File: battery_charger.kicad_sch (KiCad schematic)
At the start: 20 parts, among them J8 Conn_01x04, U15 BQ25895RTW

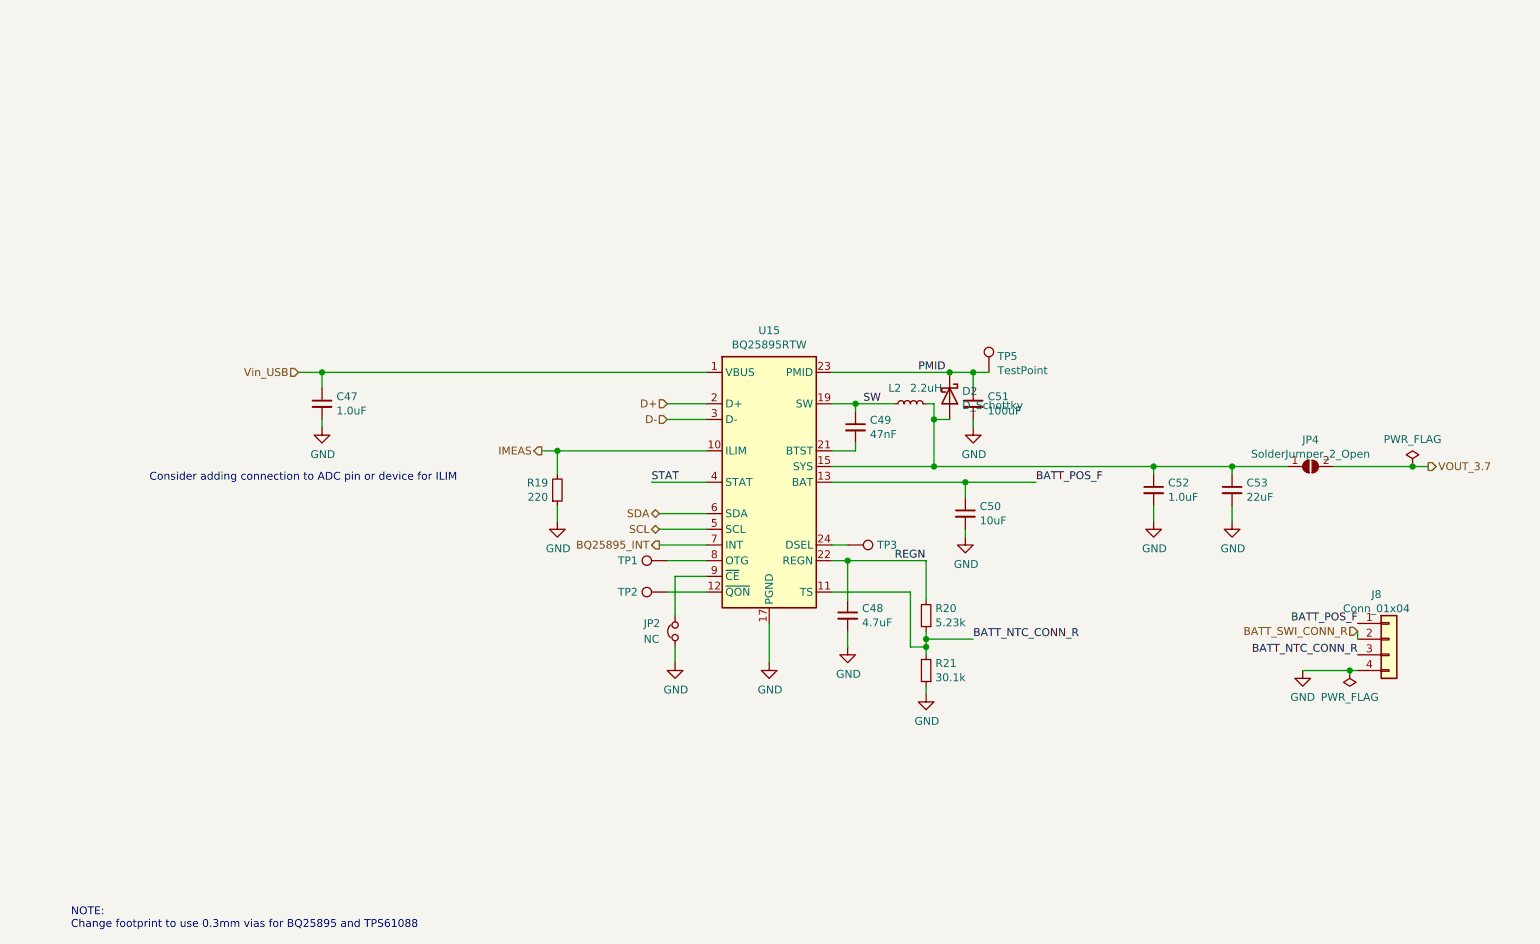
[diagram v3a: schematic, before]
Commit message: Lots of changes: add USB switch in charger circuit, reroute differential pairs using proper track widths; make CM4 courtyard the full size. Fixes #11.
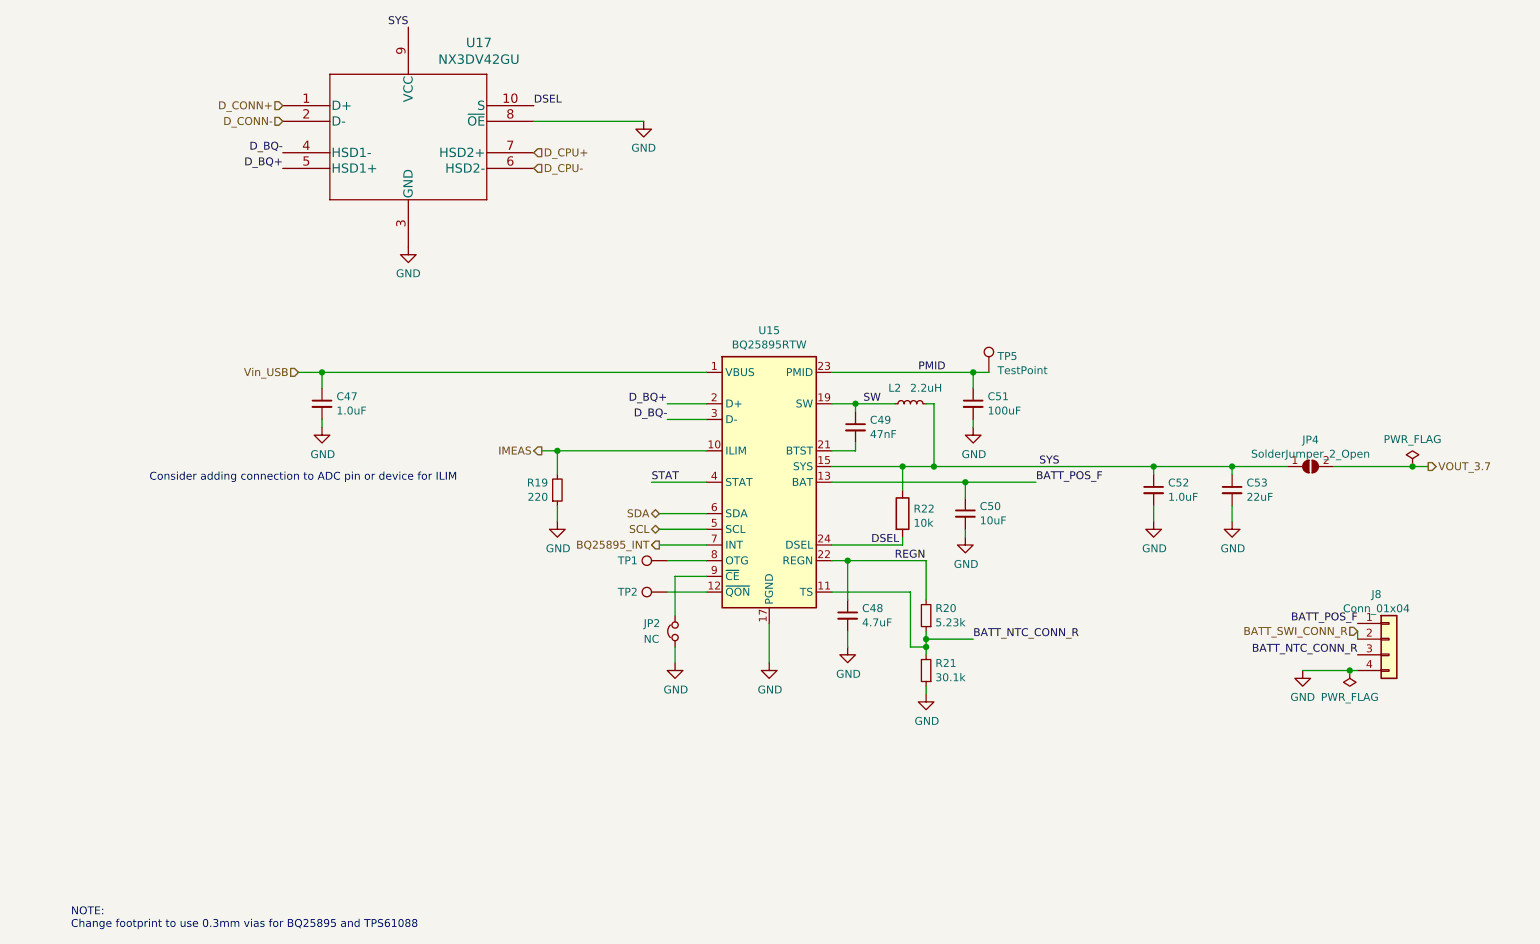
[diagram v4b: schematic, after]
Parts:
- removed D2: D_Schottky, footprints:NSR10F20NXT5G, symbol Device:D_Schottky
- removed TP3: DNP, TestPoint:TestPoint_Pad_1.0x1.0mm, symbol Connector:TestPoint
- added R22: 10k, Resistor_SMD:R_0402_1005Metric, symbol Device:R
- added U17: NX3DV42GU, footprints:NX3DV42GU, symbol NX3DV42:NX3DV42GU
- TP5: footprint (none) -> TestPoint:TestPoint_Pad_D1.0mm
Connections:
- net GND: now also U17.3 (GND), U17.8 (~OE)
- net SYS: now reaches C52.1, C53.1, JP4.1 (A), L2.2, U15.15 (SYS), U15.16 (SYS)
- net SYS: now also R22.1, U17.9 (VCC)
- net DSEL: now reaches U15.24 (DSEL)
- net DSEL: now also R22.2, U17.10 (S)
- net D+ renamed D_BQ+
- net D_BQ+: now also U17.5 (HSD1+)
- net D- renamed D_BQ-
- net D_BQ-: now also U17.4 (HSD1-)
- new net D_CONN+: U17.1 (D+)
- new net D_CONN-: U17.2 (D-)
- new net D_CPU+: U17.7 (HSD2+)
- new net D_CPU-: U17.6 (HSD2-)

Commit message: reroute LVDS diff pairs; add 5v boost converter. Fixes #1.
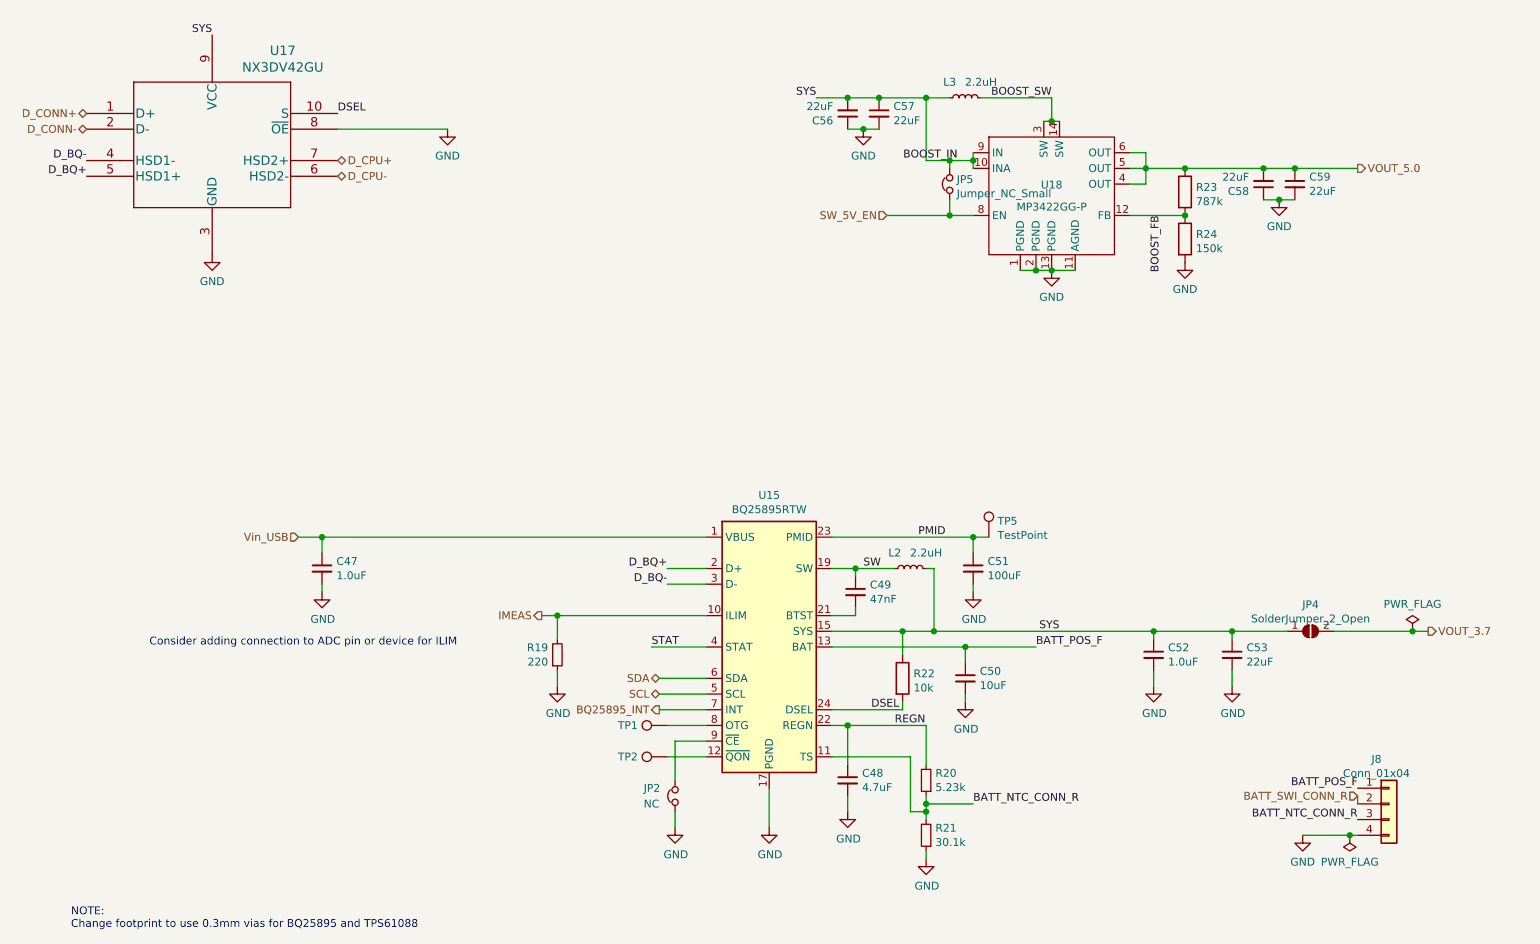
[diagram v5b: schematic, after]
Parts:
- added C56, C57, C58, C59: 22uF, Capacitor_SMD:C_0805_2012Metric, symbol Device:C_Small
- added JP5: Jumper_NC_Small, Resistor_SMD:R_0402_1005Metric, symbol Device:Jumper_NC_Small
- added L3: 2.2uH, Inductor_SMD:L_1008_2520Metric, symbol Device:L_Small
- added R23: 787k, Resistor_SMD:R_0402_1005Metric, symbol Device:R
- added R24: 150k, Resistor_SMD:R_0402_1005Metric, symbol Device:R
- added U18: MP3422GG-P, footprints:MP3422GG-P, symbol mp3422:MP3422GG-P
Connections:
- net GND: now also C56.1, C57.2, C58.1, C59.2, R24.2, U18.1 (PGND), U18.11 (AGND), U18.13 (PGND), U18.2 (PGND)
- net SYS renamed BOOST_IN
- net BOOST_IN: now also C56.2, C57.1, JP5.2, L3.1, U18.10 (INA), U18.9 (IN)
- new net BOOST_FB: R23.2, R24.1, U18.12 (FB)
- new net BOOST_SW: L3.2, U18.14 (SW), U18.3 (SW)
- new net SW_5V_EN: JP5.1, U18.8 (EN)
- new net VOUT_5.0: C58.2, C59.1, R23.1, U18.4 (OUT), U18.5 (OUT), U18.6 (OUT)
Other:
- moved on the sheet: C47, C48, C49, C50, C51, C52, C53, J8, JP2, JP4, L2, R19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

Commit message: Add datasheet for MP3422 boost converter
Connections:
- net BOOST_IN: now also JP5.1; no longer JP5.2
- net SW_5V_EN: now also JP5.2; no longer JP5.1
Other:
- moved on the sheet: JP5
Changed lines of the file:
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@@
     (pin "2")
   )
-  (symbol (lib_id "Device:Jumper_NC_Small") (at 172.72 46.99 90) (unit 1)
-    (in_bom yes) (on_board yes) (fields_autoplaced)
-    (property "Reference" "JP5" (id 0) (at 173.8631 46.2291 90)
-      (effects (font (size 1.27 1.27)) (justify right))
-    )
-    (property "Value" "Jumper_NC_Small" (id 1) (at 173.8631 48.5278 90)
-      (effects (font (size 1.27 1.27)) (justify right))
+  (symbol (lib_id "Device:Jumper_NC_Small") (at 172.72 46.99 270) (unit 1)
+    (in_bom yes) (on_board yes)
+    (property "Reference" "JP5" (id 0) (at 166.9289 46.2291 90)
+      (effects (font (size 1.27 1.27)) (justify left))
+    )
+    (property "Value" "Jumper_NC_Small" (id 1) (at 154.2289 48.5278 90)
+      (effects (font (size 1.27 1.27)) (justify left))
     )
     (property "Footprint" "Resistor_SMD:R_0402_1005Metric" (id 2) (at 172.72 46.99 0)
@@
       (effects (font (size 1.27 1.27)) hide)
     )
-    (property "Datasheet" "" (id 3) (at 189.23 49.53 0)
-      (effects (font (size 1.27 1.27)) hide)
-    )
+    (property "Datasheet" "${KIPRJMOD}/datasheets/MP3422.pdf" (id 3) (at 189.23 49.53 0)
+      (effects (font (size 1.27 1.27)) hide)
+    )

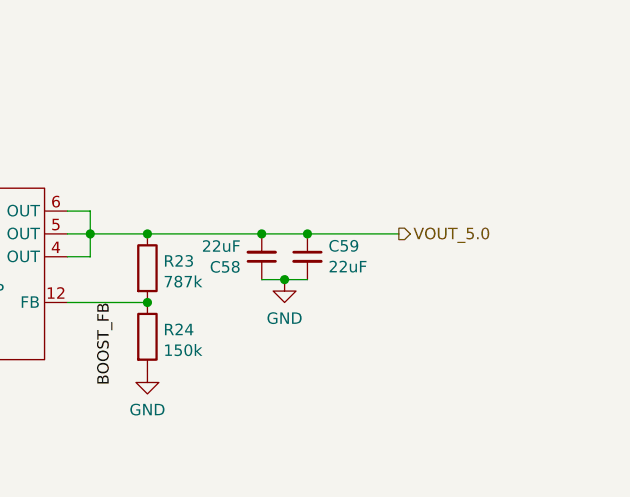
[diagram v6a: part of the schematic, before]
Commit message: Add jumper for 5V boost output.
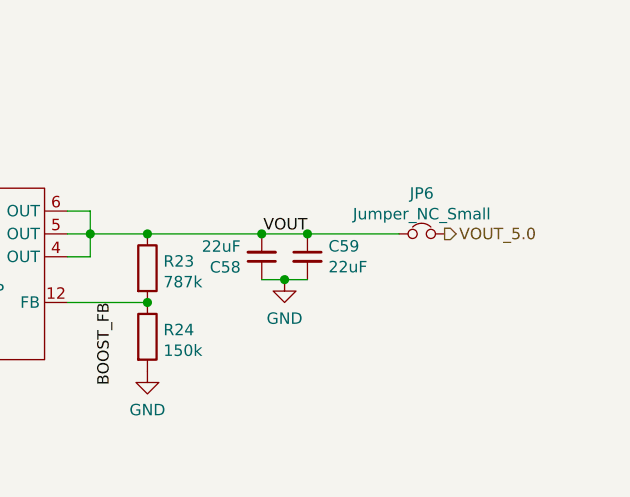
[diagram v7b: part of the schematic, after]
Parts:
- added JP6: Jumper_NC_Small, Resistor_SMD:R_0402_1005Metric, symbol Device:Jumper_NC_Small
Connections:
- net VOUT_5.0: now also JP6.2; no longer C58.2, C59.1, R23.1, U18.4 (OUT), U18.5 (OUT), U18.6 (OUT)
- new net VOUT: C58.2, C59.1, JP6.1, R23.1, U18.4 (OUT), U18.5 (OUT), U18.6 (OUT)
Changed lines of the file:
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@@
+    (effects (font (size 1.27 1.27)) (justify right bottom))
+  )
+  (label "VOUT" (at 228.6 44.45 180)
     (effects (font (size 1.27 1.27)) (justify right bottom))
   )
@@
     (effects (font (size 1.27 1.27)) (justify right))
   )
-  (hierarchical_label "VOUT_5.0" (shape output) (at 238.76 44.45 0)
+  (hierarchical_label "BATT_SWI_CONN_R" (shape input) (at 238.76 146.05 180)
+    (effects (font (size 1.27 1.27)) (justify right))
+  )
+  (hierarchical_label "VOUT_5.0" (shape output) (at 243.84 44.45 0)
     (effects (font (size 1.27 1.27)) (justify left))
-  )
-  (hierarchical_label "BATT_SWI_CONN_R" (shape input) (at 238.76 146.05 180)
-    (effects (font (size 1.27 1.27)) (justify right))
   )
   (hierarchical_label "VOUT_3.7" (shape output) (at 250.19 119.38 0)
@@
       (effects (font (size 1.27 1.27)) hide)
     )
+    (pin "1")
+    (pin "2")
+  )
+  (symbol (lib_id "Device:Jumper_NC_Small") (at 241.3 44.45 0) (unit 1)
+    (in_bom yes) (on_board yes) (fields_autoplaced)
+    (property "Reference" "JP6" (id 0) (at 241.3 39.95 0))
+    (property "Value" "Jumper_NC_Small" (id 1) (at 241.3 42.2487 0))
+    (property "Footprint" "Resistor_SMD:R_0402_1005Metric" (id 2) (at 241.3 44.45 0)
+      (effects (font (size 1.27 1.27)) hide)
+    )
+    (property "Datasheet" "~" (id 3) (at 241.3 44.45 0)
+      (effects (font (size 1.27 1.27)) hide)
+    )

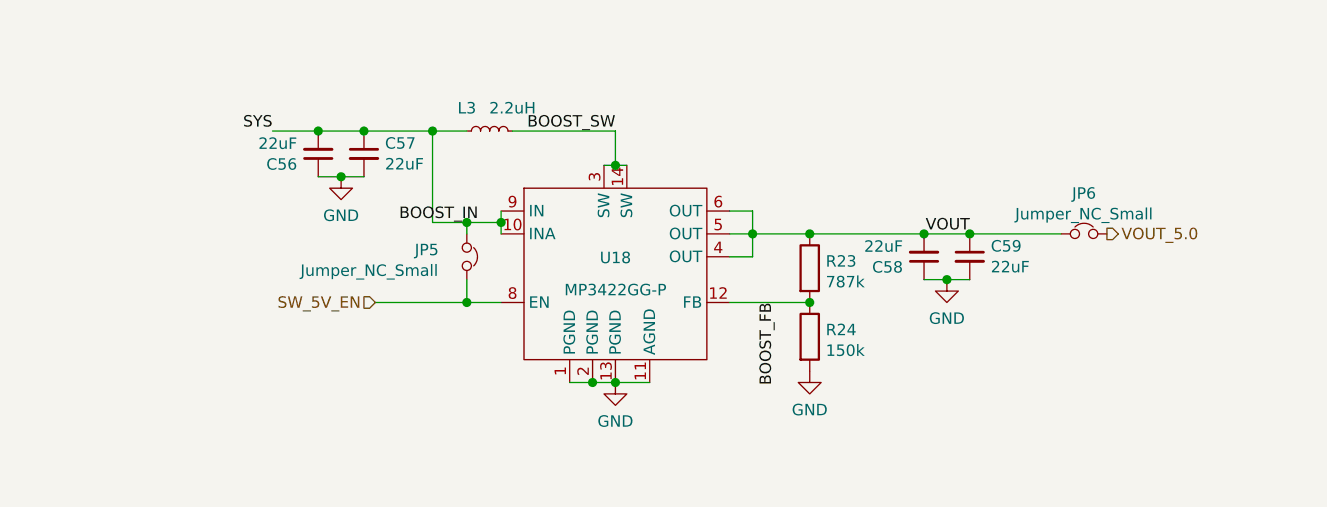
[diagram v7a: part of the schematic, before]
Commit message: Add buck-boost regulator for PCIe 3.3V
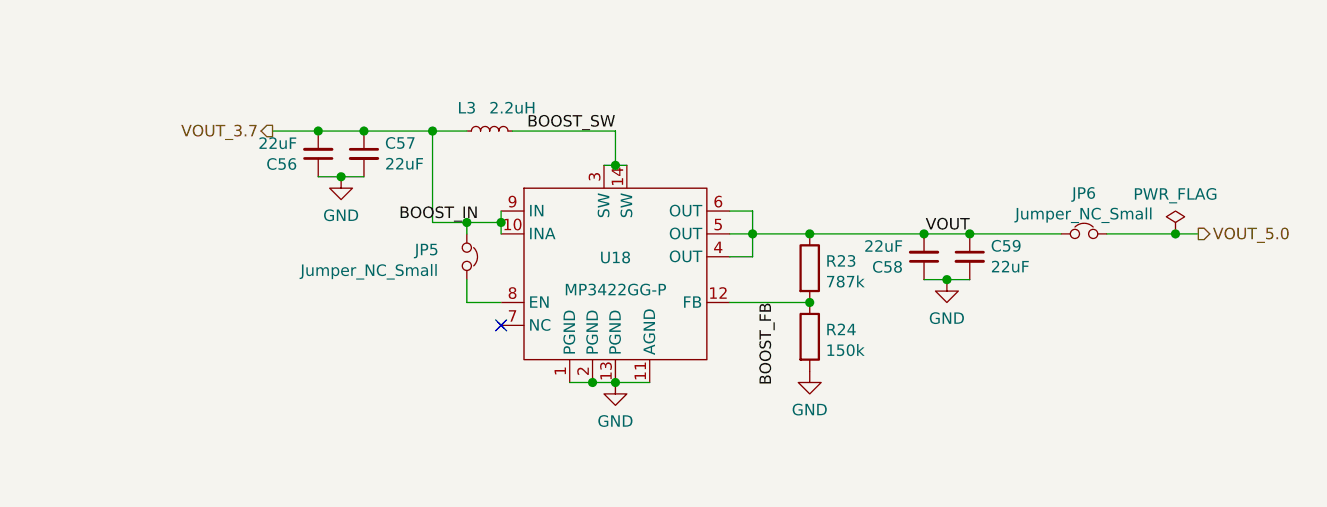
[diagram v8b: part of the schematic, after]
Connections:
- net VOUT_3.7: now also C56.2, C57.1, JP5.1, L3.1, U18.10 (INA), U18.9 (IN)
- net BOOST_IN renamed SYS
- net SYS: no longer C56.2, C57.1, JP5.1, L3.1, U18.10 (INA), U18.9 (IN)
- net SW_5V_EN: no longer names the net of JP5.2, U18.8 (EN)
- no-connect marks 0 -> 1
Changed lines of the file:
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@@
   (junction (at 170.18 119.38) (diameter 1.016) (color 0 0 0 0))
   (junction (at 172.72 43.18) (diameter 1.016) (color 0 0 0 0))
-  (junction (at 172.72 52.07) (diameter 1.016) (color 0 0 0 0))
   (junction (at 175.26 121.92) (diameter 1.016) (color 0 0 0 0))
   (junction (at 176.53 43.18) (diameter 1.016) (color 0 0 0 0))
@@
   (junction (at 237.49 152.4) (diameter 1.016) (color 0 0 0 0))
   (junction (at 247.65 119.38) (diameter 1.016) (color 0 0 0 0))
+  (junction (at 251.46 44.45) (diameter 1.016) (color 0 0 0 0))
+  (no_connect (at 176.53 54.61))
   (wire (pts (xy 67.31 104.14) (xy 71.12 104.14))
     (stroke (width 0) (type solid) (color 0 0 0 0))
@@
     (stroke (width 0) (type solid) (color 0 0 0 0))
   )
-  (wire (pts (xy 162.56 52.07) (xy 172.72 52.07))
-    (stroke (width 0) (type solid) (color 0 0 0 0))
-  )
   (wire (pts (xy 165.1 119.38) (xy 165.1 123.19))
     (stroke (width 0) (type solid) (color 0 0 0 0))
@@
   )
   (wire (pts (xy 247.65 119.38) (xy 250.19 119.38))
+    (stroke (width 0) (type solid) (color 0 0 0 0))
+  )
+  (wire (pts (xy 251.46 44.45) (xy 243.84 44.45))
+    (stroke (width 0) (type solid) (color 0 0 0 0))
+  )
+  (wire (pts (xy 254 44.45) (xy 251.46 44.45))
     (stroke (width 0) (type solid) (color 0 0 0 0))
   )
@@
     (effects (font (size 1.27 1.27)) (justify right bottom))
   )
-  (label "SYS" (at 151.13 33.02 180)
-    (effects (font (size 1.27 1.27)) (justify right bottom))
-  )
   (label "SW" (at 158.75 109.22 0)
     (effects (font (size 1.27 1.27)) (justify left bottom))
@@
     (effects (font (size 1.27 1.27)) (justify right))
   )
-  (hierarchical_label "SW_5V_EN" (shape input) (at 162.56 52.07 180)
+  (hierarchical_label "VOUT_3.7" (shape output) (at 151.13 33.02 180)
     (effects (font (size 1.27 1.27)) (justify right))
   )
@@
     (effects (font (size 1.27 1.27)) (justify right))
   )
-  (hierarchical_label "VOUT_5.0" (shape output) (at 243.84 44.45 0)
+  (hierarchical_label "VOUT_3.7" (shape output) (at 250.19 119.38 0)
     (effects (font (size 1.27 1.27)) (justify left))
   )
-  (hierarchical_label "VOUT_3.7" (shape output) (at 250.19 119.38 0)
+  (hierarchical_label "VOUT_5.0" (shape output) (at 254 44.45 0)
     (effects (font (size 1.27 1.27)) (justify left))
   )
@@
     )
     (property "Datasheet" "~" (id 3) (at 247.65 119.38 0)
+      (effects (font (size 1.27 1.27)) hide)
+    )
+    (pin "1")
+  )
+  (symbol (lib_id "power:PWR_FLAG") (at 251.46 44.45 0) (unit 1)
+    (in_bom yes) (on_board yes)
+    (property "Reference" "#FLG0103" (id 0) (at 251.46 42.545 0)
+      (effects (font (size 1.27 1.27)) hide)
+    )
+    (property "Value" "PWR_FLAG" (id 1) (at 251.46 40.0558 0))
+    (property "Footprint" "" (id 2) (at 251.46 44.45 0)
+      (effects (font (size 1.27 1.27)) hide)
+    )
+    (property "Datasheet" "~" (id 3) (at 251.46 44.45 0)
       (effects (font (size 1.27 1.27)) hide)
     )
@@
     (pin "5")
     (pin "6")
+    (pin "7")
     (pin "8")
     (pin "9")
